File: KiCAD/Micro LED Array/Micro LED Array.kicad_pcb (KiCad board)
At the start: 2 copper layers, 8.7 x 7.5 mm, 113 parts

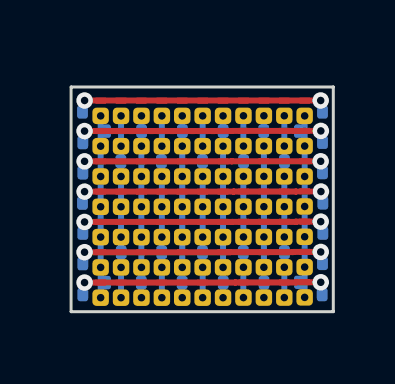
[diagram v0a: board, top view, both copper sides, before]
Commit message: Driver board connected, add interboard fiducials
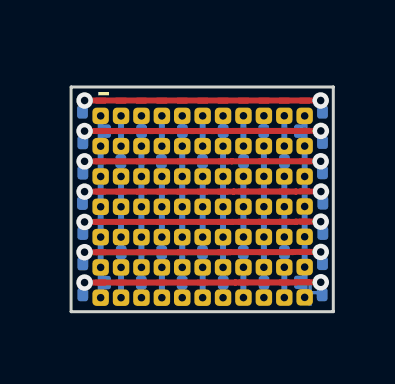
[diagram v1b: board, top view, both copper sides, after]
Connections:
- D1 pad 2: /Col1 -> /Col7
- D10 pad 2: /Col3 -> /Col5
- D12 pad 2: /Col5 -> /Col3
- D13 pad 2: /Col6 -> /Col2
- D14 pad 2: /Col7 -> /Col1
- D15 pad 2: /Col1 -> /Col7
- D16 pad 2: /Col2 -> /Col6
- D17 pad 2: /Col3 -> /Col5
- D19 pad 2: /Col5 -> /Col3
- D2 pad 2: /Col2 -> /Col6
- D20 pad 2: /Col6 -> /Col2
- D21 pad 2: /Col7 -> /Col1
- D22 pad 2: /Col1 -> /Col7
- D23 pad 2: /Col2 -> /Col6
- D24 pad 2: /Col3 -> /Col5
- D26 pad 2: /Col5 -> /Col3
- D27 pad 2: /Col6 -> /Col2
- D28 pad 2: /Col7 -> /Col1
- D29 pad 2: /Col1 -> /Col7
- D3 pad 2: /Col3 -> /Col5
- D30 pad 2: /Col2 -> /Col6
- D31 pad 2: /Col3 -> /Col5
- D33 pad 2: /Col5 -> /Col3
- D34 pad 2: /Col6 -> /Col2
- D35 pad 2: /Col7 -> /Col1
- D36 pad 2: /Col1 -> /Col7
- D37 pad 2: /Col2 -> /Col6
- D38 pad 2: /Col3 -> /Col5
- D40 pad 2: /Col5 -> /Col3
- D41 pad 2: /Col6 -> /Col2
- D42 pad 2: /Col7 -> /Col1
- D43 pad 2: /Col1 -> /Col7
- D44 pad 2: /Col2 -> /Col6
- D45 pad 2: /Col3 -> /Col5
- D47 pad 2: /Col5 -> /Col3
- D48 pad 2: /Col6 -> /Col2
- D49 pad 2: /Col7 -> /Col1
- D5 pad 2: /Col5 -> /Col3
- D6 pad 2: /Col6 -> /Col2
- D7 pad 2: /Col7 -> /Col1
- D8 pad 2: /Col1 -> /Col7
- D9 pad 2: /Col2 -> /Col6
- H15 pad 1: /Col1 -> /Col7
- H16 pad 1: /Col1 -> /Col7
- H17 pad 1: /Col2 -> /Col6
- H18 pad 1: /Col2 -> /Col6
- H19 pad 1: /Col3 -> /Col5
- H20 pad 1: /Col3 -> /Col5
- H23 pad 1: /Col5 -> /Col3
- H24 pad 1: /Col5 -> /Col3
- H25 pad 1: /Col6 -> /Col2
- H26 pad 1: /Col6 -> /Col2
- H27 pad 1: /Col7 -> /Col1
- H28 pad 1: /Col7 -> /Col1
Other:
- board text added: "+"
- board text added: "-"

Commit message: Fix LED array 0201 footprint for centroid file for assembly
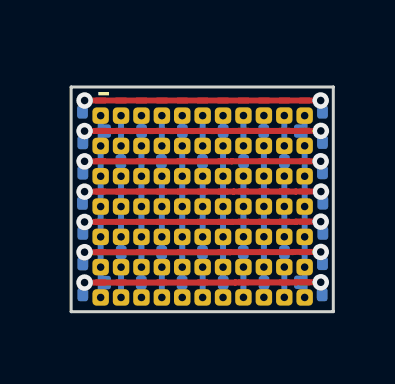
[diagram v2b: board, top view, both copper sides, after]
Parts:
- turned D15 to 0 degrees
- turned D16 to 0 degrees
- turned D17 to 0 degrees
- turned D18 to 0 degrees
- turned D19 to 0 degrees
- turned D20 to 0 degrees
- turned D21 to 0 degrees
- turned D22 to 0 degrees
- turned D23 to 0 degrees
- turned D24 to 0 degrees
- turned D25 to 0 degrees
- turned D26 to 0 degrees
- turned D27 to 0 degrees
- turned D28 to 0 degrees
- turned D36 to 0 degrees
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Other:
- board text removed: "+"
